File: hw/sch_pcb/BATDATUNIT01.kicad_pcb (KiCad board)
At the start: 2 copper layers, 136.2 x 85.9 mm, 222 parts, among them J1 USBC_USB4105-GF-A, J2 SD_Card-FPS009-4200-0, J3 HEADER_2x03, J4 46436-9327, Q1 BC817-25, Q2 BC817-25, Q3 BC817-25, Q4 BC817-25, Q5 BC817-25, Q6 BC817-25, Q7 BSS83P, SW1 SKRTLAE010, SW2 KMT031, SW3 SKRTLAE010, SW4 KMT031, U1 MAX14502AETL+, U10 PCF85263A, U11 TCA4307, U12 BQ34Z100, U13 BQ25628E, U14 SN74HC164P, U15 TPS631000DRLR, U16 TPS631000DRLR, U17 TPS631000DRLR, U18 TPS22965-Q1, U2 USBLC6-2SC6, U4 PCA9541ABS/01, U5 AT24CS64-SSHM, U6 SHT35-DIS, U7 TMUX1574DYYR, U8 ATMEGA1284P-AU, U9 MS561101BA03-50, Y1 19.2 MHz, Y2 8 MHz, Y3 ABS07-120-32.768KHZ-T

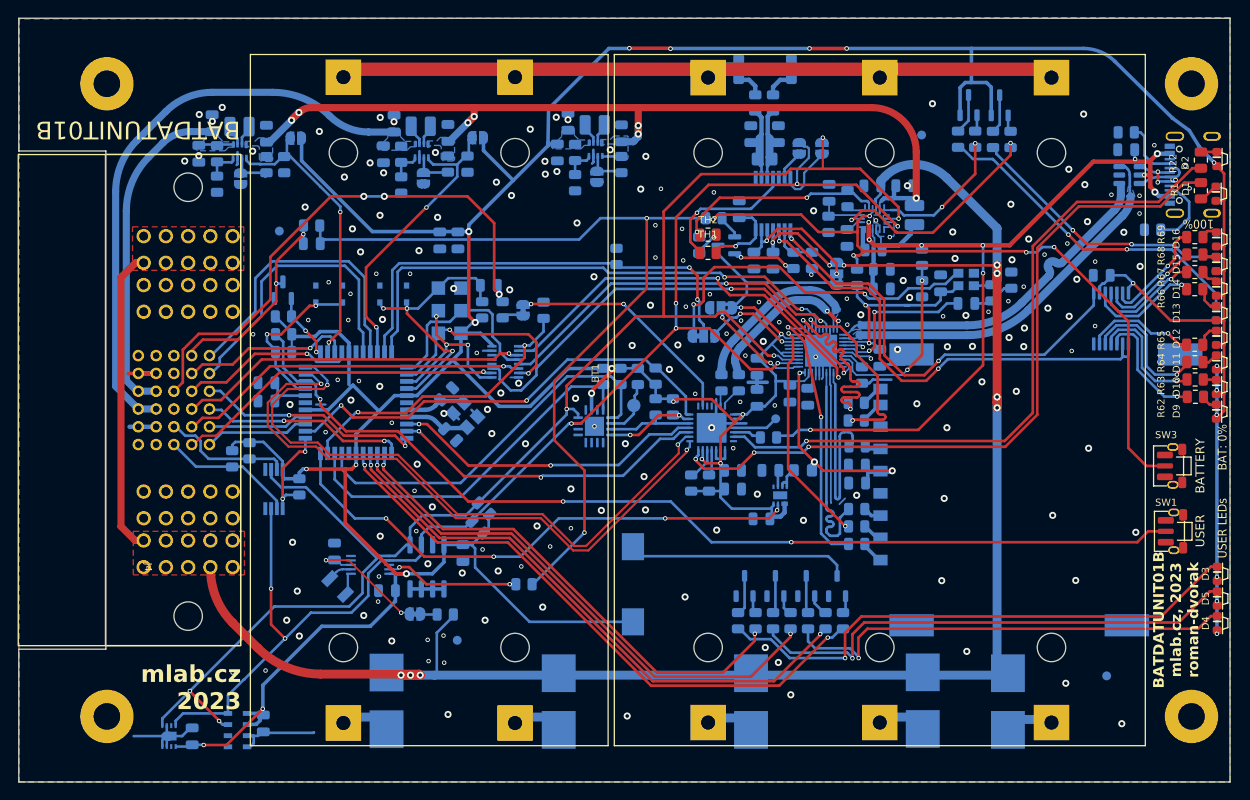
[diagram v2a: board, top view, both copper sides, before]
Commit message: Fix poor power connection under MCU.
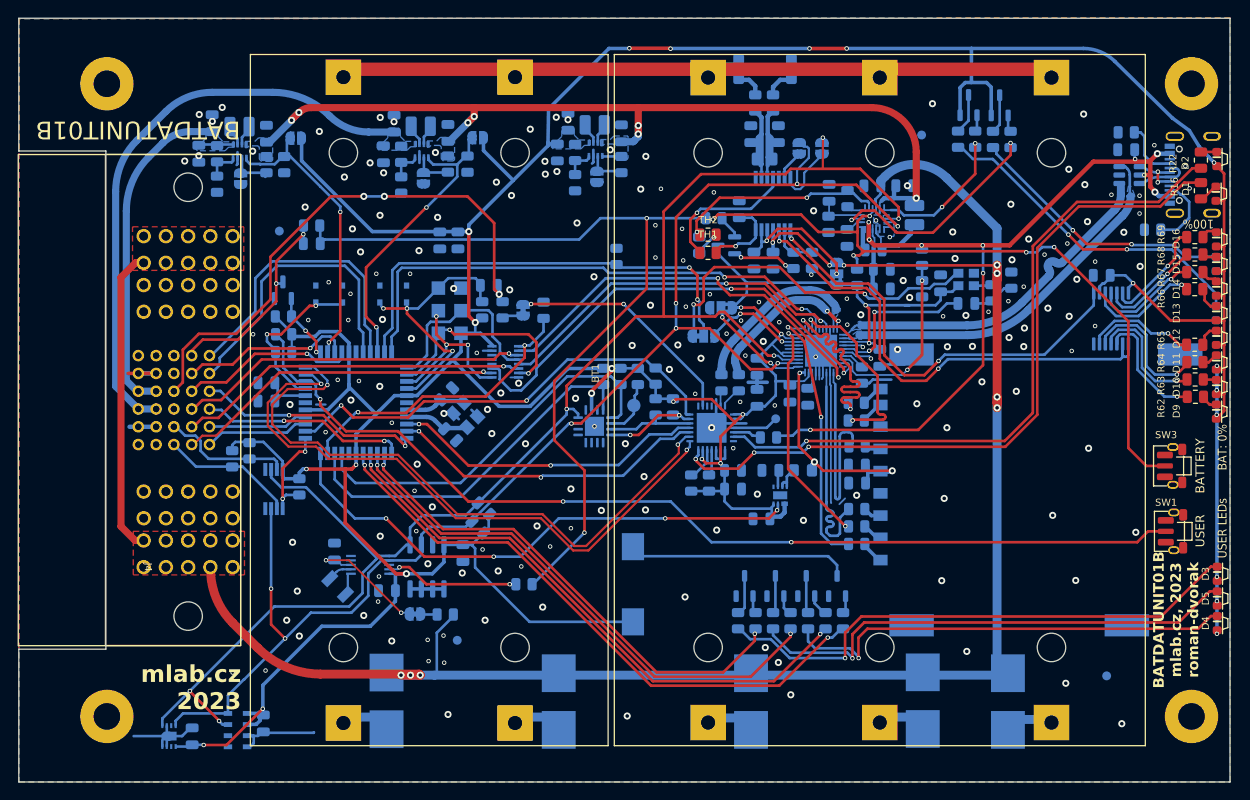
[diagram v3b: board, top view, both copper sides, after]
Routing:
- net Net-(JP3-A): track 2.09 -> 2.76 mm

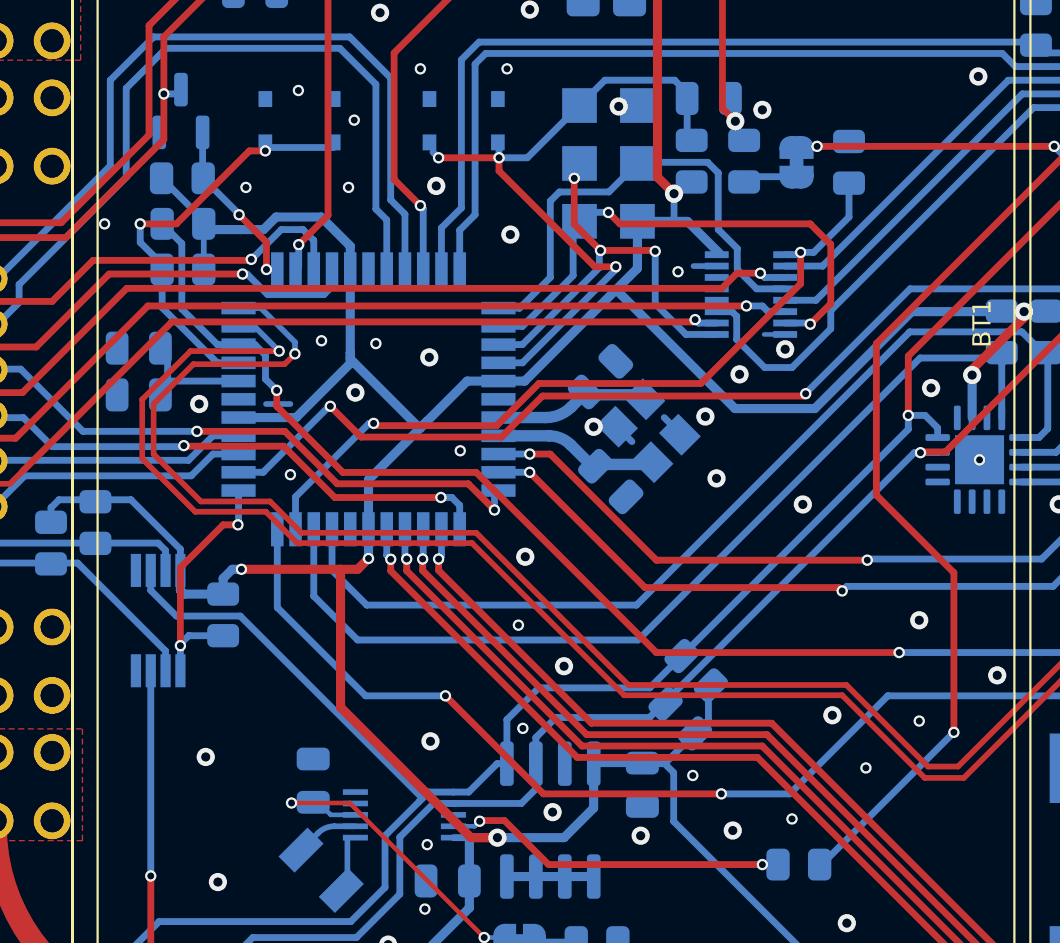
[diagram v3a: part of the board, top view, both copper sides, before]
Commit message: Connect the RTC time-stamp input to USER A button.
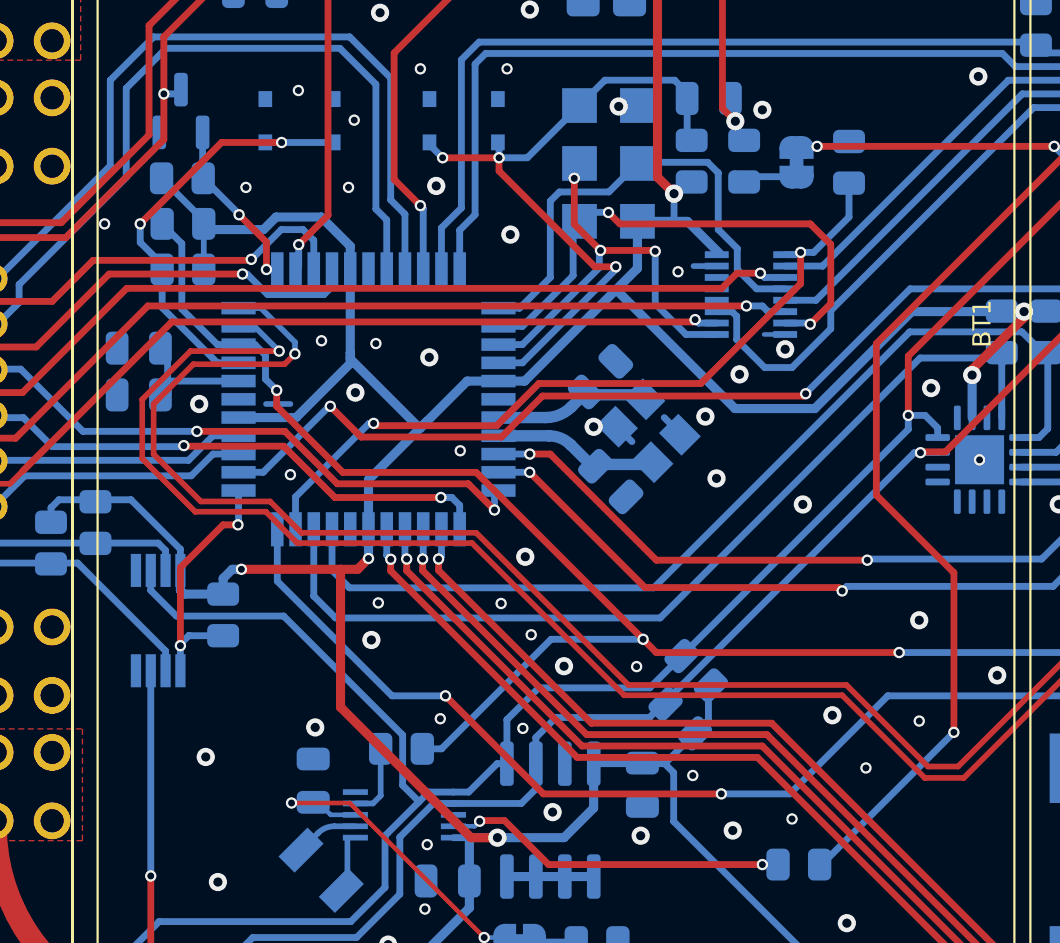
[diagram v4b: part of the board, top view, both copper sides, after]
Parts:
- added R82: 100R, Resistor_SMD:R_0805_2012Metric, B.Cu at (122.1, 120.6)
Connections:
- U10 pad 4: unconnected-(U10-TS-Pad4) -> Net-(U10-TS)
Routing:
- net /BTN_USER_A: track 113.0 -> 124.6 mm, vias 3 -> 4
- net Net-(U10-TS): track 0.00 -> 3.31 mm
- net SDA_I2C: track 170.6 -> 171.8 mm
- net /SDA_MCU: track 42.0 -> 41.2 mm
- net 3v3_SD_CTRL: track 61.1 -> 60.4 mm
- net /BTN_USER_B: track 18.1 -> 18.8 mm
- net /SCL_MCU: track 43.7 -> 43.1 mm
- net GND: vias 190 -> 195

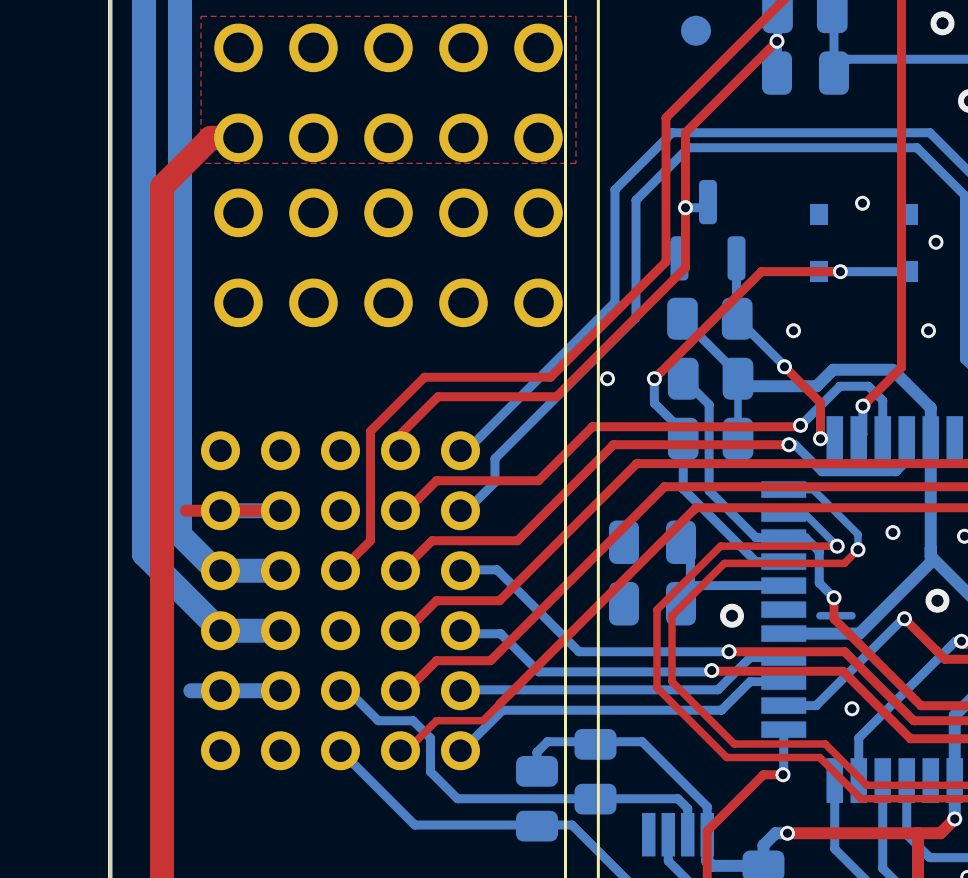
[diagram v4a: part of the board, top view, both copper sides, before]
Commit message: Change diode D6 to decrease leakage current.
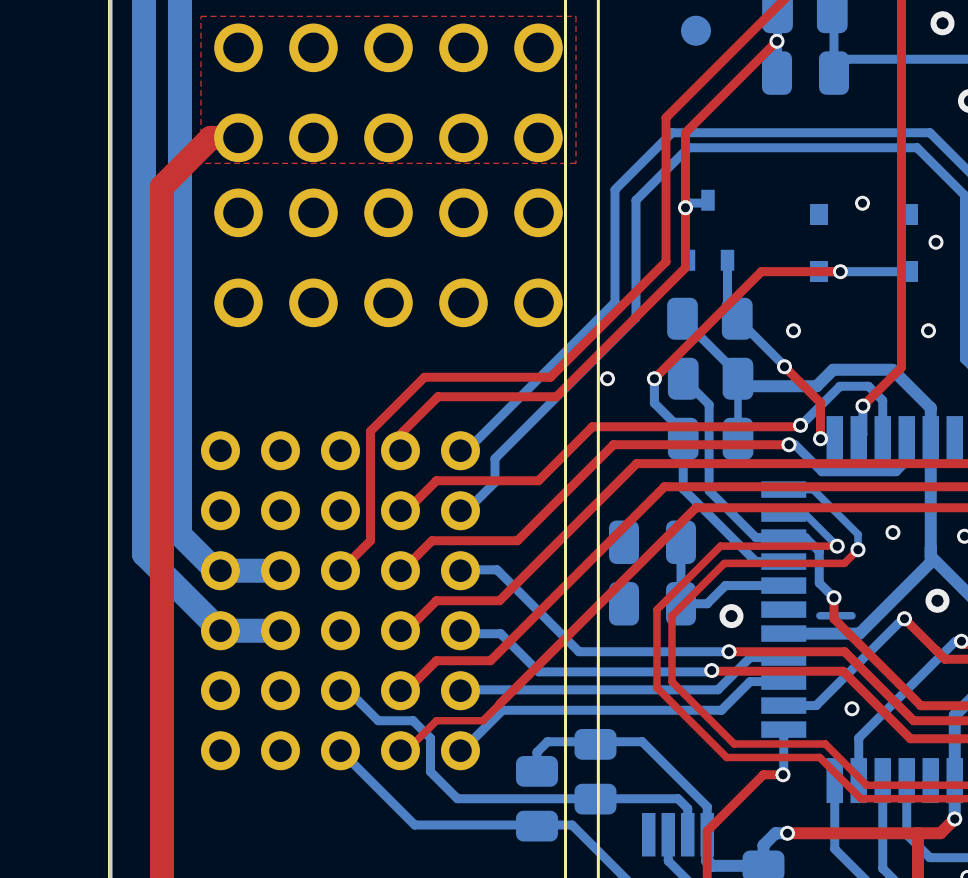
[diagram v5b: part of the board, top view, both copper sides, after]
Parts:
- D6: value BAS70-04 -> BAS16W; footprint Package_TO_SOT_SMD:SOT-23 -> Package_TO_SOT_SMD:SOT-323_SC-70
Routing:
- net GND: track 91.1 -> 82.5 mm
- net Net-(U8-AREF): track 4.56 -> 5.73 mm
